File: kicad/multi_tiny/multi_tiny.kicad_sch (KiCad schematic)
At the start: 55 parts, among them J1 Conn_02x03_Odd_Even, J2 28pin ZIF, J8 Conn_01x25, SW1 SW_SPDT, SW2 SW_SPDT, SW3 SW_SPDT, SW4 SW_SPST, U1 CD4052B, U2 CD4052B, U3 CD4052B, U4 CD4052B

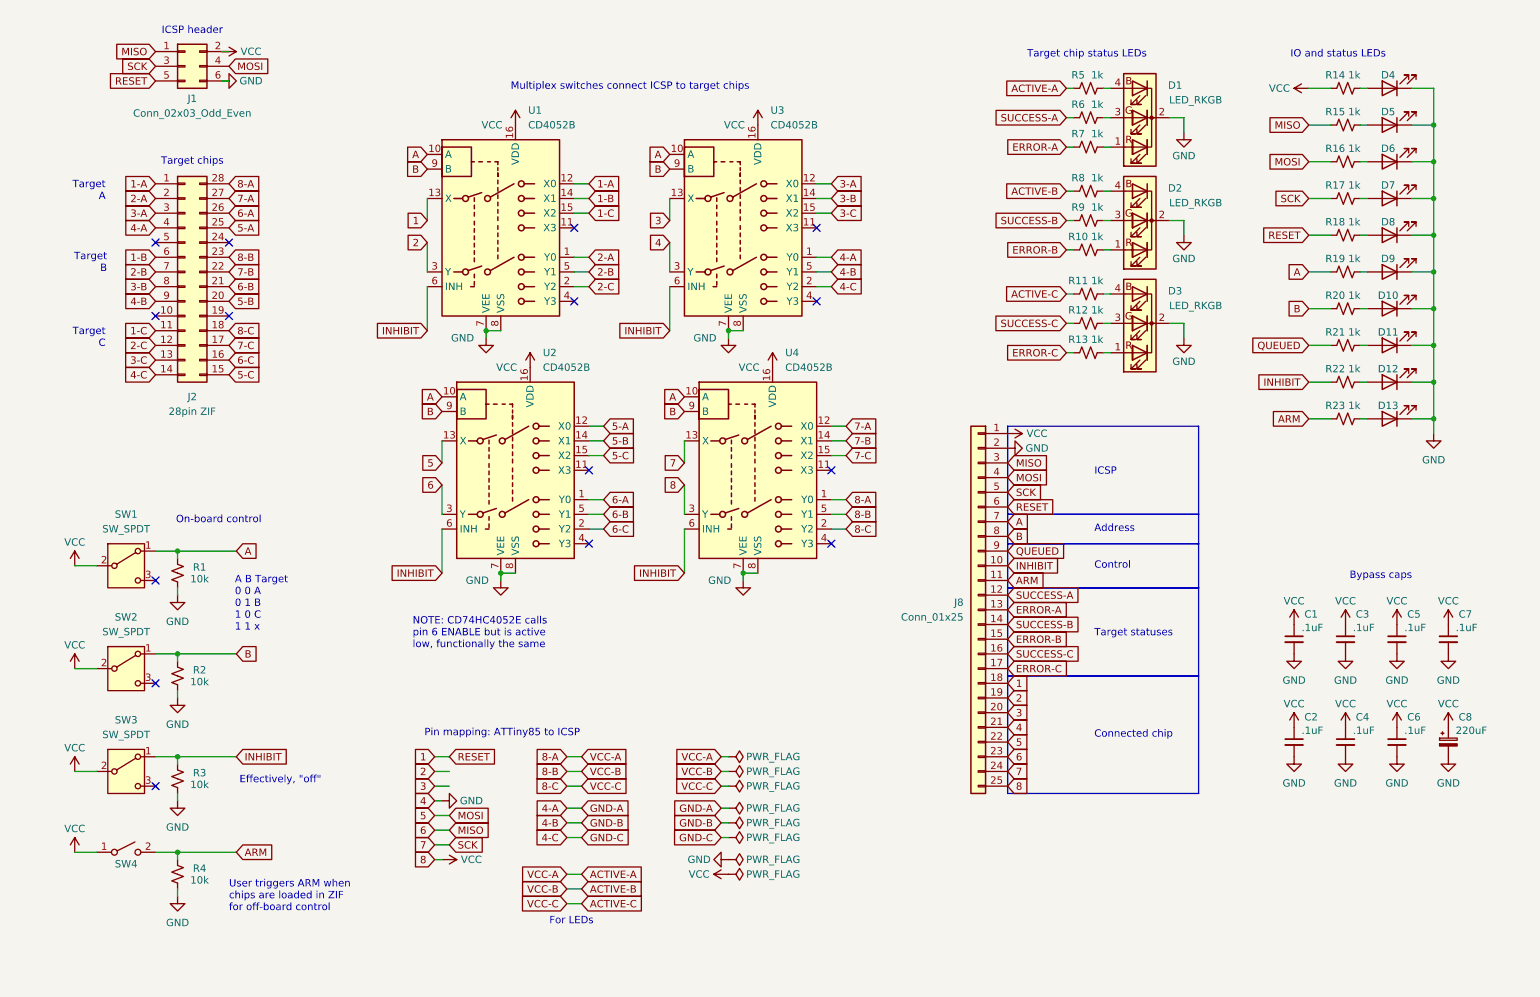
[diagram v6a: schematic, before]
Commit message: Re-layout for flanked ZIF
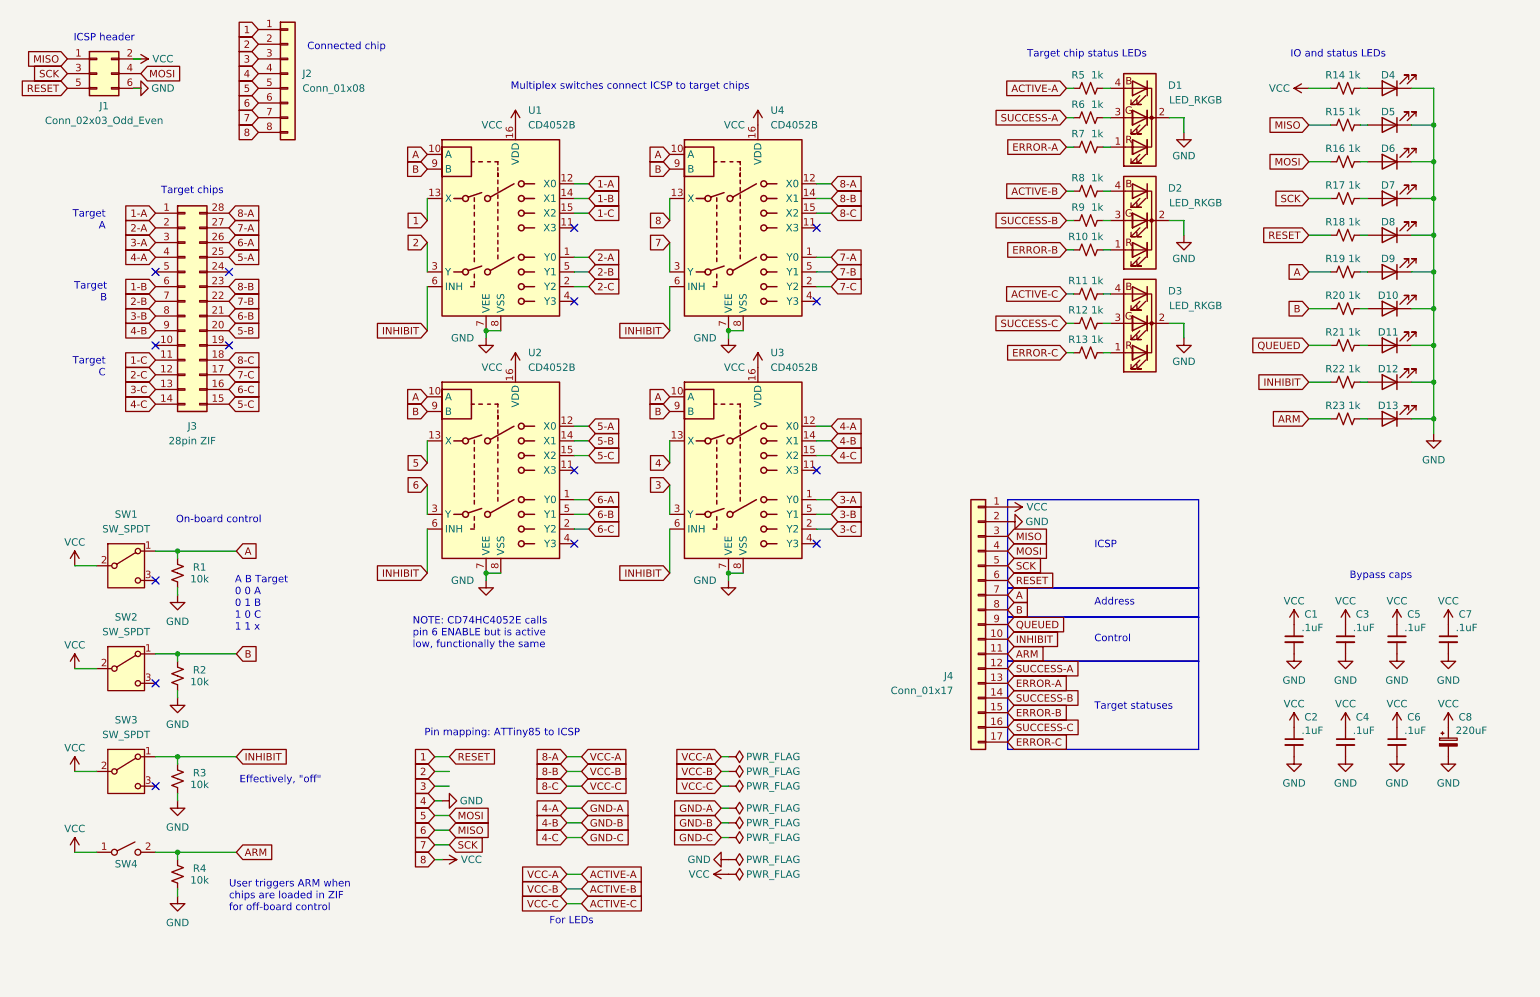
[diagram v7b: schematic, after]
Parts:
- removed J8: Conn_01x25, Connector_PinSocket_2.54mm:PinSocket_1x25_P2.54mm_Vertical, symbol Connector_Generic:Conn_01x25
- added J2: Conn_01x08, Connector_PinHeader_2.54mm:PinHeader_1x08_P2.54mm_Vertical, symbol Connector_Generic:Conn_01x08
- added J4: Conn_01x17, Connector_PinHeader_2.54mm:PinHeader_1x17_P2.54mm_Vertical, symbol Connector_Generic:Conn_01x17
- renumbered J2 to J3
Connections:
- net 1: now also J2.1 (Pin_1), J4.6 (Pin_6)
- net 2: now also J2.2 (Pin_2)
- net 3: now also U3.3 (Y), J2.3 (Pin_3); no longer U3.13 (X)
- net 3-A: now also U3.1 (Y0); no longer U3.12 (X0)
- net 3-B: now also U3.5 (Y1); no longer U3.14 (X1)
- net 3-C: now also U3.2 (Y2); no longer U3.15 (X2)
- net 4-A: now also U3.12 (X0); no longer U3.1 (Y0)
- net 4-B: now also U3.14 (X1); no longer U3.5 (Y1)
- net 4-C: now also U3.15 (X2); no longer U3.2 (Y2)
- net 5: now also J2.5 (Pin_5), J4.4 (Pin_4)
- net 6: now also J2.6 (Pin_6), J4.3 (Pin_3)
- net 7: now also U4.3 (Y), J2.7 (Pin_7), J4.5 (Pin_5); no longer U4.13 (X)
- net 7-A: now also U4.1 (Y0); no longer U4.12 (X0)
- net 7-B: now also U4.5 (Y1); no longer U4.14 (X1)
- net 7-C: now also U4.2 (Y2); no longer U4.15 (X2)
- net 8-A: now also U4.12 (X0); no longer U4.1 (Y0)
- net 8-B: now also U4.14 (X1); no longer U4.5 (Y1)
- net 8-C: now also U4.15 (X2); no longer U4.2 (Y2)
- net A: now also J4.7 (Pin_7)
- net ARM: now also J4.11 (Pin_11)
- net B: now also J4.8 (Pin_8)
- net ERROR-A: now also J4.13 (Pin_13)
- net ERROR-B: now also J4.15 (Pin_15)
- net ERROR-C: now also J4.17 (Pin_17)
- net GND: now also U3.13 (X), J2.4 (Pin_4), J4.2 (Pin_2); no longer U3.3 (Y)
- net INHIBIT: now also J4.10 (Pin_10)
- net QUEUED: now also J4.9 (Pin_9)
- net SUCCESS-A: now also J4.12 (Pin_12)
- net SUCCESS-B: now also J4.14 (Pin_14)
- net SUCCESS-C: now also J4.16 (Pin_16)
- net VCC: now also U4.13 (X), J2.8 (Pin_8), J4.1 (Pin_1); no longer U4.3 (Y)
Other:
- moved on the sheet: J1, J3, U2, U3, U4

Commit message: Re-layout
* Fix ZIF dimensions
* IO refinements: ditch inhibit switch, pullups
  on external controls, add clear button
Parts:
- removed R4: 10k, Resistor_THT:R_Axial_DIN0207_L6.3mm_D2.5mm_P10.16mm_Horizontal, symbol Device:R_Small_US
- removed SW3: SW_SPDT, Button_Switch_THT:SW_Slide_SPDT_Straight_CK_OS102011MS2Q, symbol Switch:SW_SPDT
- added SW5: SW_SPST, Button_Switch_THT:SW_PUSH_6mm, symbol Switch:SW_SPST
- D11: value QUEUED -> ARM
- D12: value INHIBIT -> CLEAR
- D13: value ARM -> INHIBIT
- J3: footprint Socket:DIP_Socket-28_W6.9_W7.62_W10.16_W12.7_W13.5_3M_228-4817-00-0602J -> Package_DIP:DIP-28_W7.62mm_LongPads
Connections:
- net QUEUED is gone; now on net ARM: J4.9 (Pin_9), R21.1
- net ARM: no longer J4.11 (Pin_11), R23.1
- net INHIBIT: now also J4.11 (Pin_11), R23.1; no longer J4.10 (Pin_10), R22.1
- net VCC: now also SW5.1 (A)
- new net CLEAR: J4.10 (Pin_10), R22.1, SW5.2 (B)
- no-connect marks 15 -> 14
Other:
- note added: "For off-board control: * ARM when ZIF is loaded * CLEAR when open or to reset target statuses"
- note removed: "Effectively, "off""
- note removed: "User triggers ARM when chips are loaded in ZIF for off-board control"
- moved on the sheet: R3, SW4
